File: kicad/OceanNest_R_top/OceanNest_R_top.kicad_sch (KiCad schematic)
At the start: 35 parts, among them J21 Conn_01x07_Pin, J22 TRRS_MJ-4PP-9, SW21 SW_PUSH, SW22 SW_PUSH, SW23 SW_PUSH, SW24 SW_PUSH, SW25 SW_PUSH, SW26 SW_PUSH, SW27 SW_PUSH, SW28 SW_PUSH, SW29 SW_PUSH, SW30 SW_PUSH, SW31 SW_PUSH, SW32 SW_PUSH, SW33 SW_PUSH, SW34 SW_PUSH, SW35 SW_PUSH, SW36 SW_PUSH, U21 RP2040-Zero

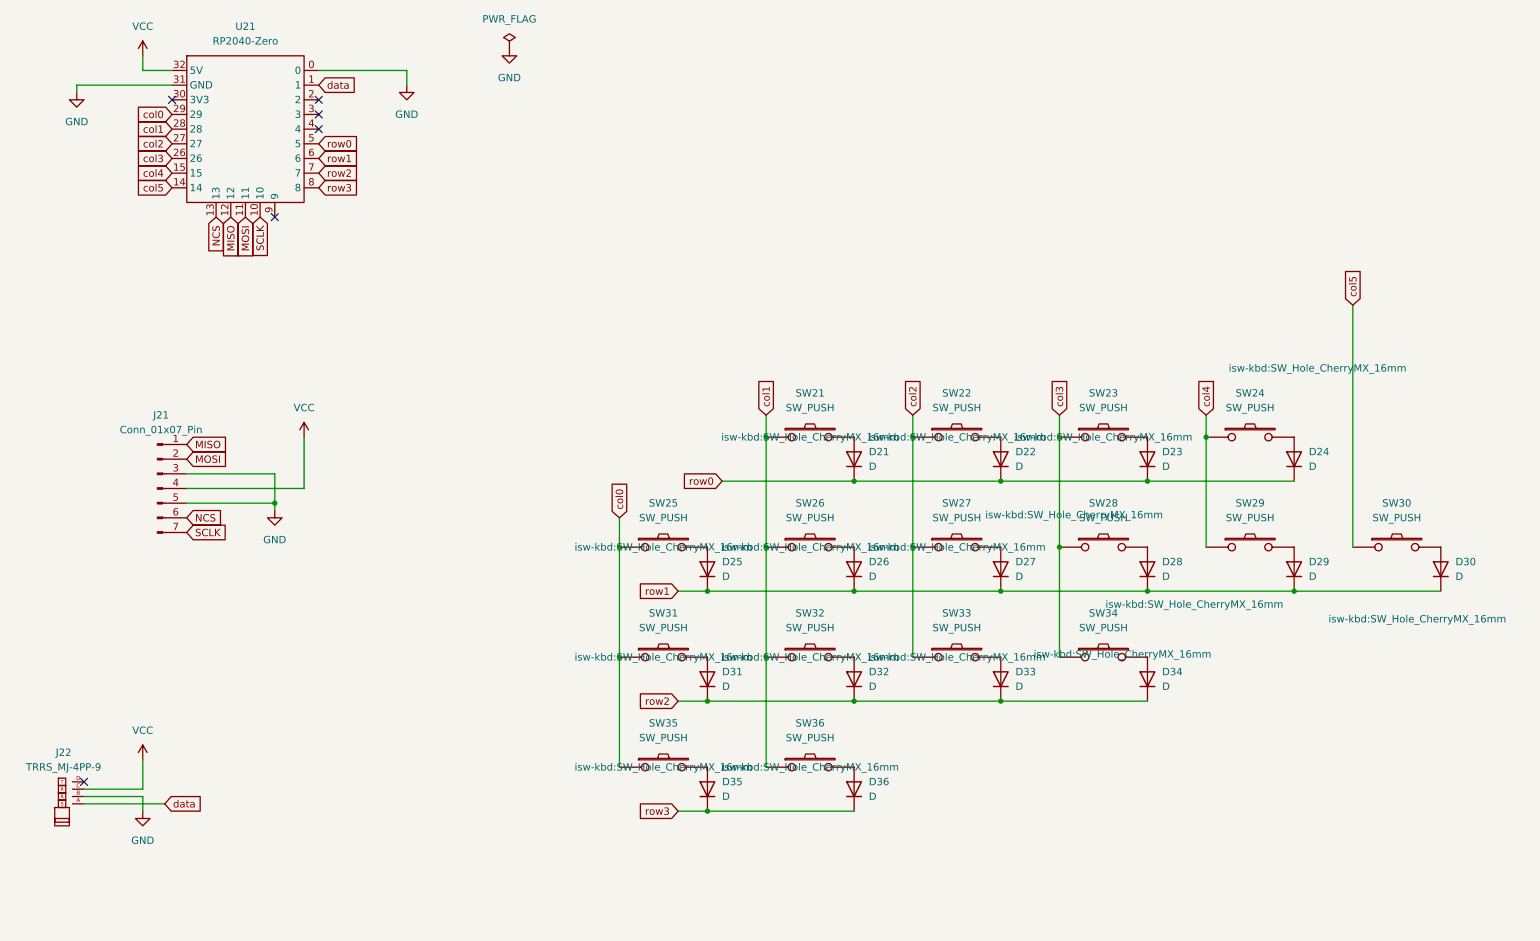
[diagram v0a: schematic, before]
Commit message: feat: update PCB and schematic files for OceanNest project, including new components and layout adjustments
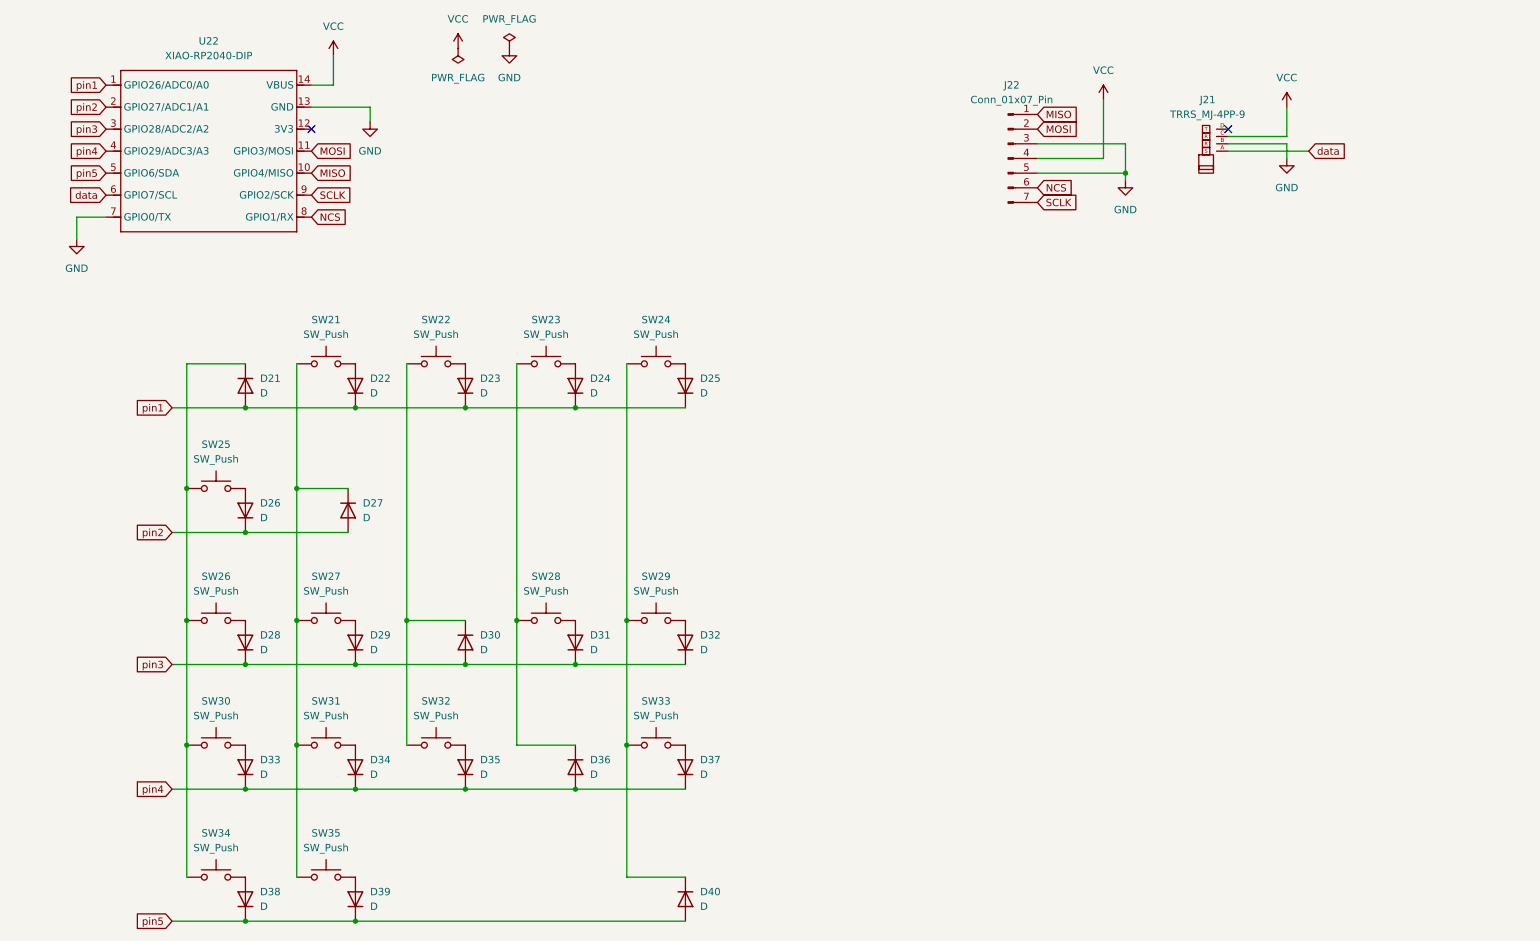
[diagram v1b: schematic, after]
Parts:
- removed SW21, SW22, SW23, SW24, SW25, SW26, SW27, SW28, SW29, SW30, SW31, SW32, SW33, SW34, SW35, SW36: SW_PUSH, isw-kbd:SW_Hole_CherryMX_16mm, symbol kbd:SW_PUSH
- removed U21: RP2040-Zero, isw-kbd:RP2040-Zero, symbol isw-mcu:RP2040-Zero
- added D37, D38, D39, D40: D, kbd_Parts:Diode_SMD, symbol Device:D
- added SW21, SW22, SW23, SW24, SW25, SW26, SW27, SW28, SW29, SW30, SW31, SW32, SW33, SW34, SW35: SW_Push, takashicompany:CherryMX_Hotswap_16m, symbol Switch:SW_Push
- added U22: XIAO-RP2040-DIP, xiao_rp2040:XIAO-RP2040-DIP, symbol xiao_rp2040:XIAO-RP2040-DIP
- D21, D22, D23, D24, D25, D26, D27, D28, D29, D30, D31, D32, D33, D34, D35, D36: footprint (none) -> kbd_Parts:Diode_SMD
- renumbered J22 to J21, J21 to J22
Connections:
- net GND: now also U22.13 (GND), U22.7 (GPIO0/TX)
- net MISO: now also U22.10 (GPIO4/MISO)
- net MOSI: now also U22.11 (GPIO3/MOSI)
- net NCS: now also U22.8 (GPIO1/RX)
- net SCLK: now also U22.9 (GPIO2/SCK)
- net VCC: now also U22.14 (VBUS)
- net data: now also U22.6 (GPIO7/SCL)
- net at D29.2 (A): now also SW27.2
- net at D33.2 (A): now also SW30.2
- net pin4: now reaches D36.2 (A)
- net pin4: now also D33.1 (K), D34.1 (K), D35.1 (K), D37.1 (K), U22.4 (GPIO29/ADC3/A3)
- net at D31.2 (A): now also SW28.2
- net at D22.2 (A): now also SW21.2
- net pin1: now reaches D21.2 (A)
- net pin1: now also D22.1 (K), D23.1 (K), D24.1 (K), D25.1 (K), U22.1 (GPIO26/ADC0/A0)
- net at D28.2 (A): now also SW26.2
- net at D23.2 (A): now also SW22.2
- net pin3: now reaches D30.2 (A)
- net pin3: now also D28.1 (K), D29.1 (K), D31.1 (K), D32.1 (K), U22.3 (GPIO28/ADC2/A2)
- net at D35.2 (A): now also SW32.2
- net at D24.2 (A): now also SW23.2
- net at D26.2 (A): now also SW25.2
- net at D34.2 (A): now also SW31.2
- net at D25.2 (A): now also SW24.2
- net at D32.2 (A): now also SW29.2
- net pin2: now reaches D27.2 (A)
- net pin2: now also D26.1 (K), U22.2 (GPIO27/ADC1/A1)
- removed net row0: D21.1 (K), D22.1 (K), D23.1 (K), D24.1 (K)
- removed net row1: D25.1 (K), D26.1 (K), D27.1 (K), D28.1 (K), D29.1 (K), D30.1 (K)
- removed net row2: D31.1 (K), D32.1 (K), D33.1 (K), D34.1 (K)
- net row3: no longer names the net of D36.1 (K)
- net row3: now also SW23.1, SW28.1; no longer D35.1 (K)
- new net: D40.1 (K), SW24.1, SW29.1, SW33.1
- new net: D37.2 (A), SW33.2
- new net: D38.2 (A), SW34.2
- new net: D21.1 (K), SW25.1, SW26.1, SW30.1, SW34.1
- new net: D27.1 (K), SW21.1, SW27.1, SW31.1, SW35.1
- new net: D30.1 (K), SW22.1, SW32.1
- new net: D39.2 (A), SW35.2
- new net pin5: D38.1 (K), D39.1 (K), D40.2 (A), U22.5 (GPIO6/SDA)
- no-connect marks 6 -> 2
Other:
- moved on the sheet: J21, J22
